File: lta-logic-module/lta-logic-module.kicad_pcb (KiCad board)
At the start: 2 copper layers, 63 parts, among them J1 Conn_01x01_Female, J2 Conn_01x01_Female, J3 Conn_01x12, J4 Conn_01x12, J5 Conn_01x12, U1 Feather_M4_Express, U10 PCF8574, U11 PCF8574, U12 PCF8574, U2 LM2595T-5, U3 SN74LVC14AD, U4 SN74LVC14AD, U5 SN74LVC00AD, U6 SN74LVC00AD, U7 SN74LVC244AN, U8 SN74LVC00AD, U9 SN74LVC00AD

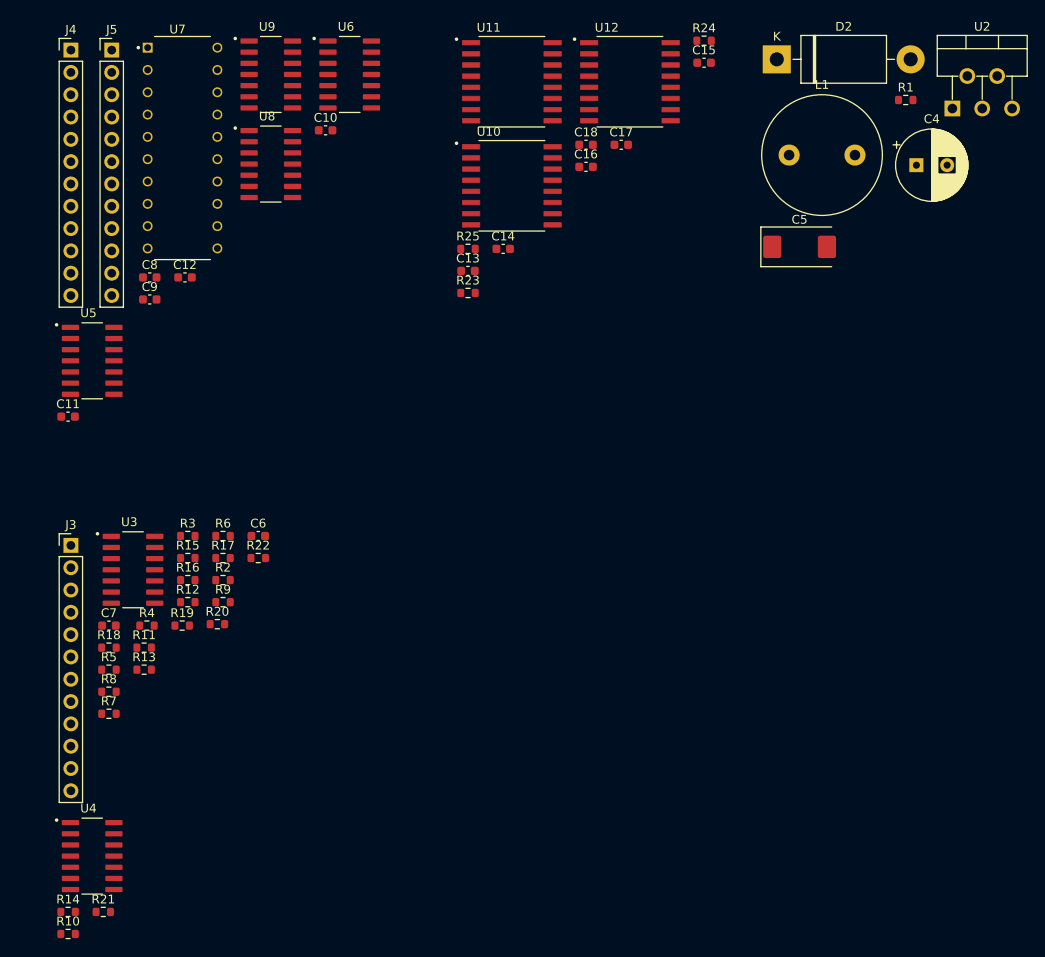
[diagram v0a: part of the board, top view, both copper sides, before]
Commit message: Initial PCB setup
* Configure Elecrow DRC checks for lta-logic-module.
* Switch SN74LVC244A from 'N' PDIP to 'DWR' SOIC footprint.
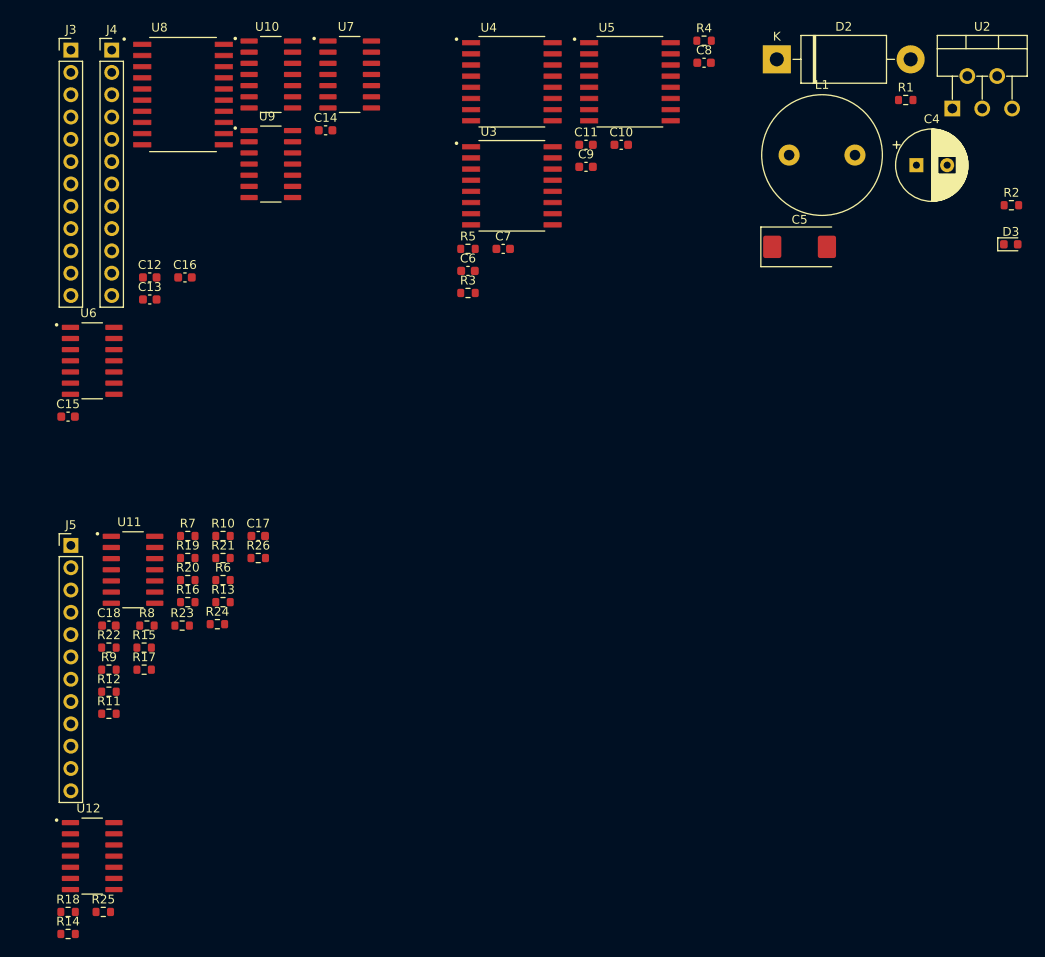
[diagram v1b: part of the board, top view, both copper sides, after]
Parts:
- removed the U7 at (131.9, 69.3)
- added D3: PWR (RED), LED_SMD:LED_0603_1608Metric, F.Cu at (226.2, 80.3)
- added R2: 330R, Resistor_SMD:R_0603_1608Metric, F.Cu at (226.2, 75.8)
- added U8: SN74LVC244ADW, Aaron_TI_Parts:TI_SOIC_DW0020A, F.Cu at (131.9, 63.2)
- renumbered C17 to C10, C18 to C11, C8 to C12, C9 to C13, C10 to C14, C11 to C15, C12 to C16, C6 to C17, C7 to C18, C13 to C6, C14 to C7, C15 to C8, C16 to C9, J4 to J3, J5 to J4, J3 to J5, R6 to R10, R7 to R11, R8 to R12, R9 to R13, R10 to R14, R11 to R15, R12 to R16, R13 to R17, R14 to R18, R15 to R19, R16 to R20, R17 to R21, R18 to R22, R19 to R23, R20 to R24, R21 to R25, R22 to R26, R23 to R3, R24 to R4, R25 to R5, R2 to R6, R3 to R7, R4 to R8, R5 to R9, U9 to U10, U3 to U11, U4 to U12, U10 to U3, U11 to U4, U12 to U5, U5 to U6, U6 to U7, U8 to U9

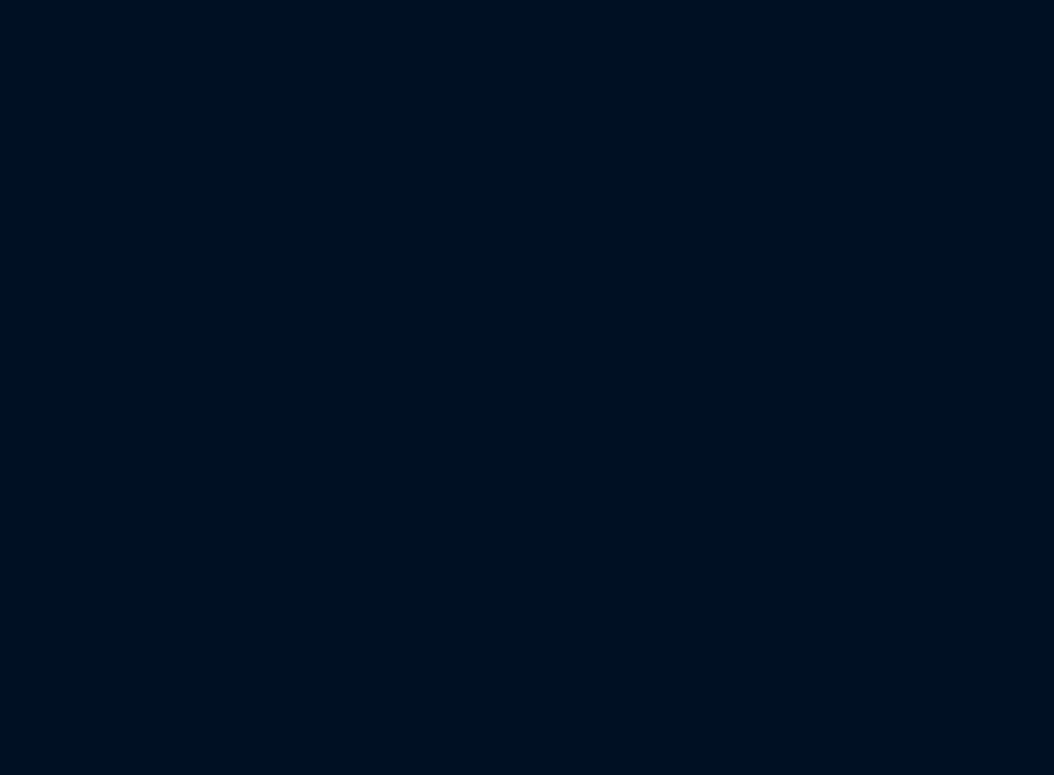
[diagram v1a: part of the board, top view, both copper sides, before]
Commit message: Add light sensor circuit.
Adjust TODOs and comments after testing btn circuit.
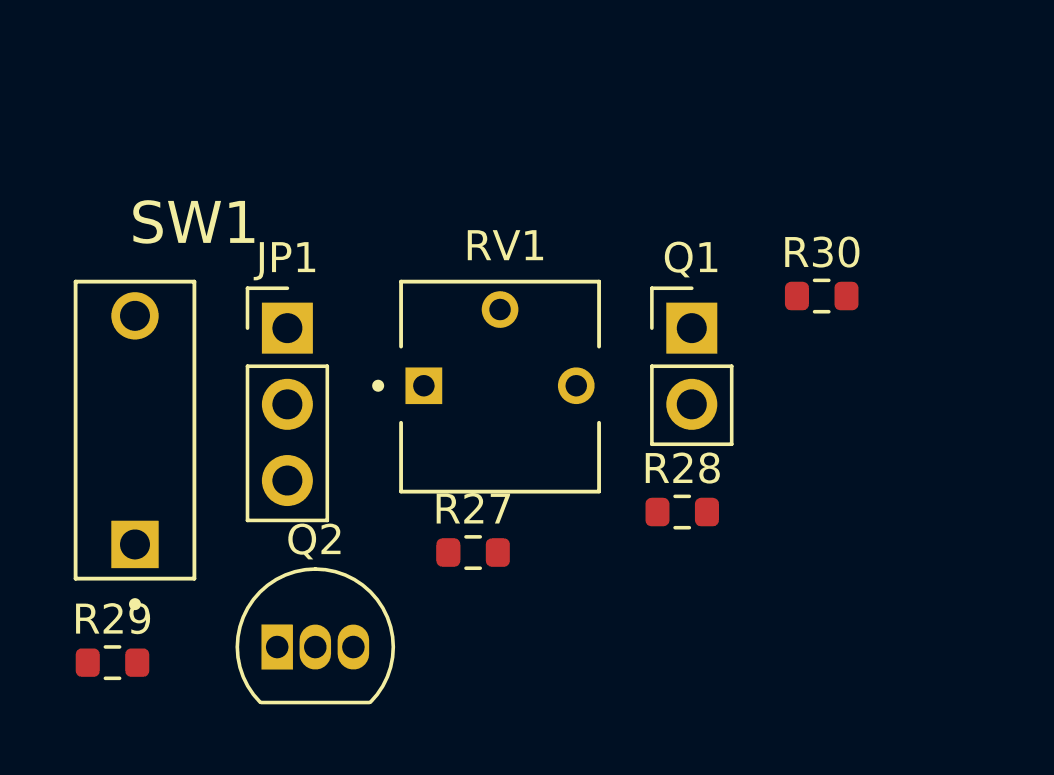
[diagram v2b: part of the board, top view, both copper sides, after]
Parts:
- added JP1: Jumper_3_Open, Connector_PinHeader_2.54mm:PinHeader_1x03_P2.54mm_Vertical, F.Cu at (58.8, 146.5)
- added Q1: PT334-6B, Connector_PinHeader_2.54mm:PinHeader_1x02_P2.54mm_Vertical, F.Cu at (72.2, 146.5)
- added Q2: KSC945CYTA, Package_TO_SOT_THT:TO-92_Inline, F.Cu at (58.4, 157.1)
- added R27: 4K7, Resistor_SMD:R_0603_1608Metric, F.Cu at (64.9, 154.0)
- added R28: 470R, Resistor_SMD:R_0603_1608Metric, F.Cu at (71.9, 152.6)
- added R29: 220R, Resistor_SMD:R_0603_1608Metric, F.Cu at (52.9, 157.7)
- added R30: 4K7, Resistor_SMD:R_0603_1608Metric, F.Cu at (76.6, 145.4)
- added RV1: 25K, Aaron_THT:TRIM_3362P, F.Cu at (65.8, 148.4)
- added SW1: SW_SPST, Aaron_THT:CUI-DIP-SW_DS01-254-x-01xx, F.Cu at (53.7, 149.9)
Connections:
- U1 pad 9: unconnected-(U1-Pad9) -> /DARK

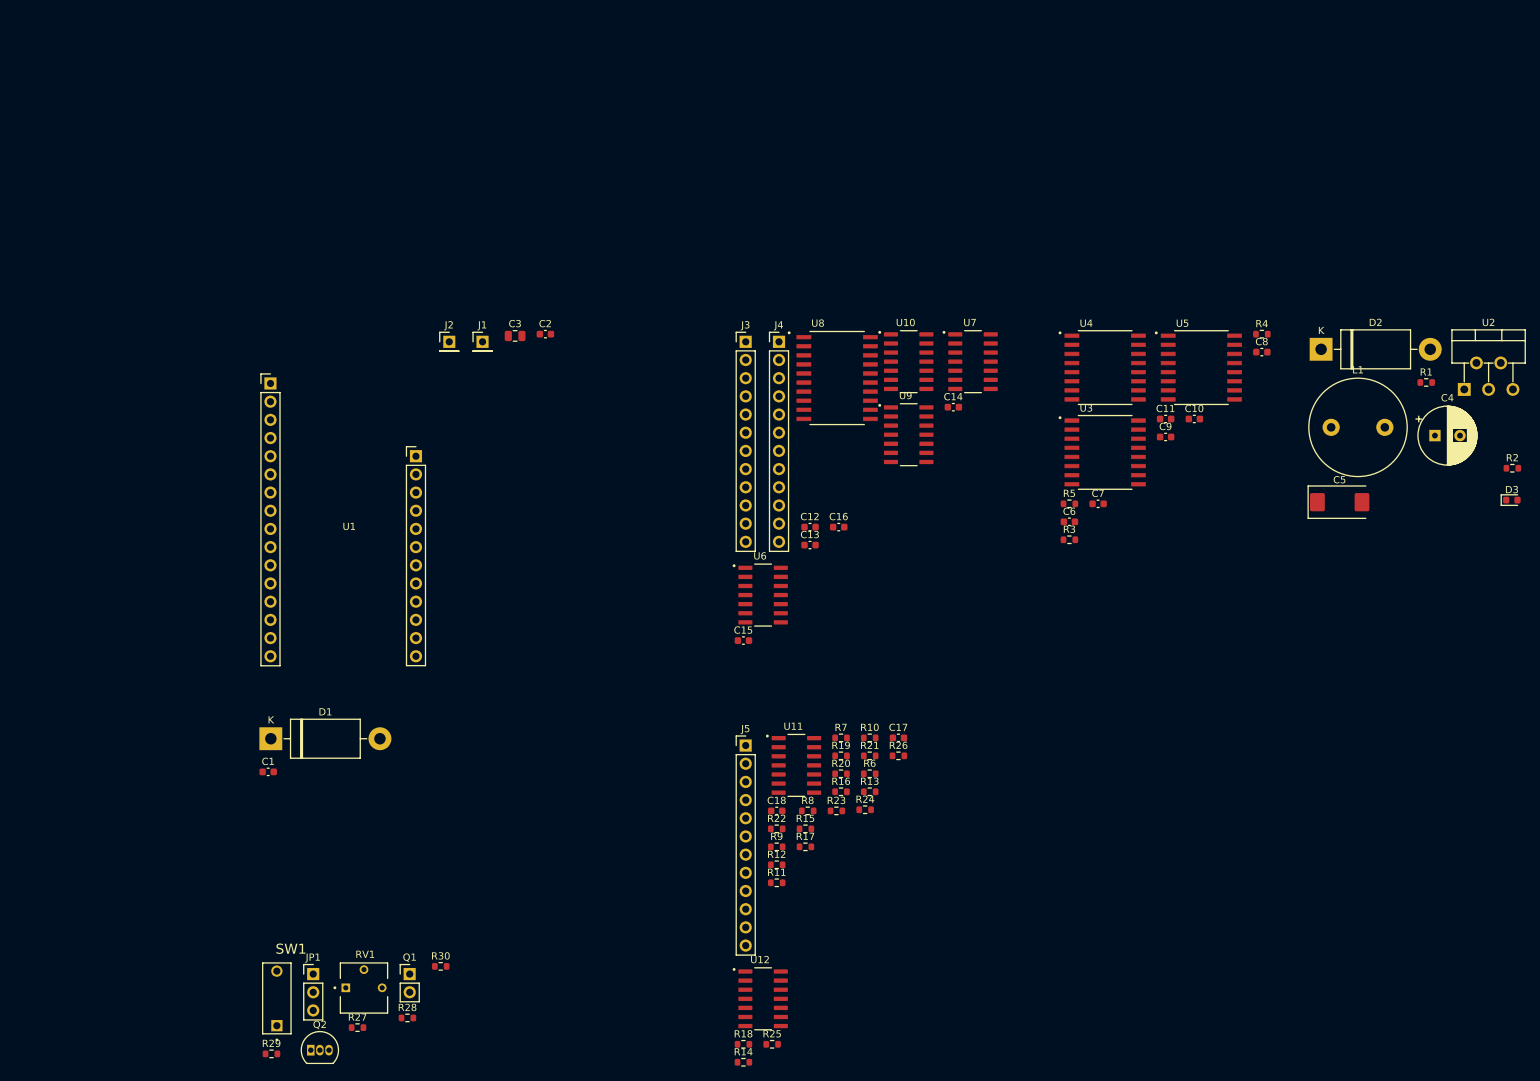
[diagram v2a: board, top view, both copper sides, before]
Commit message: Add main draft of PCB layout for logic module.
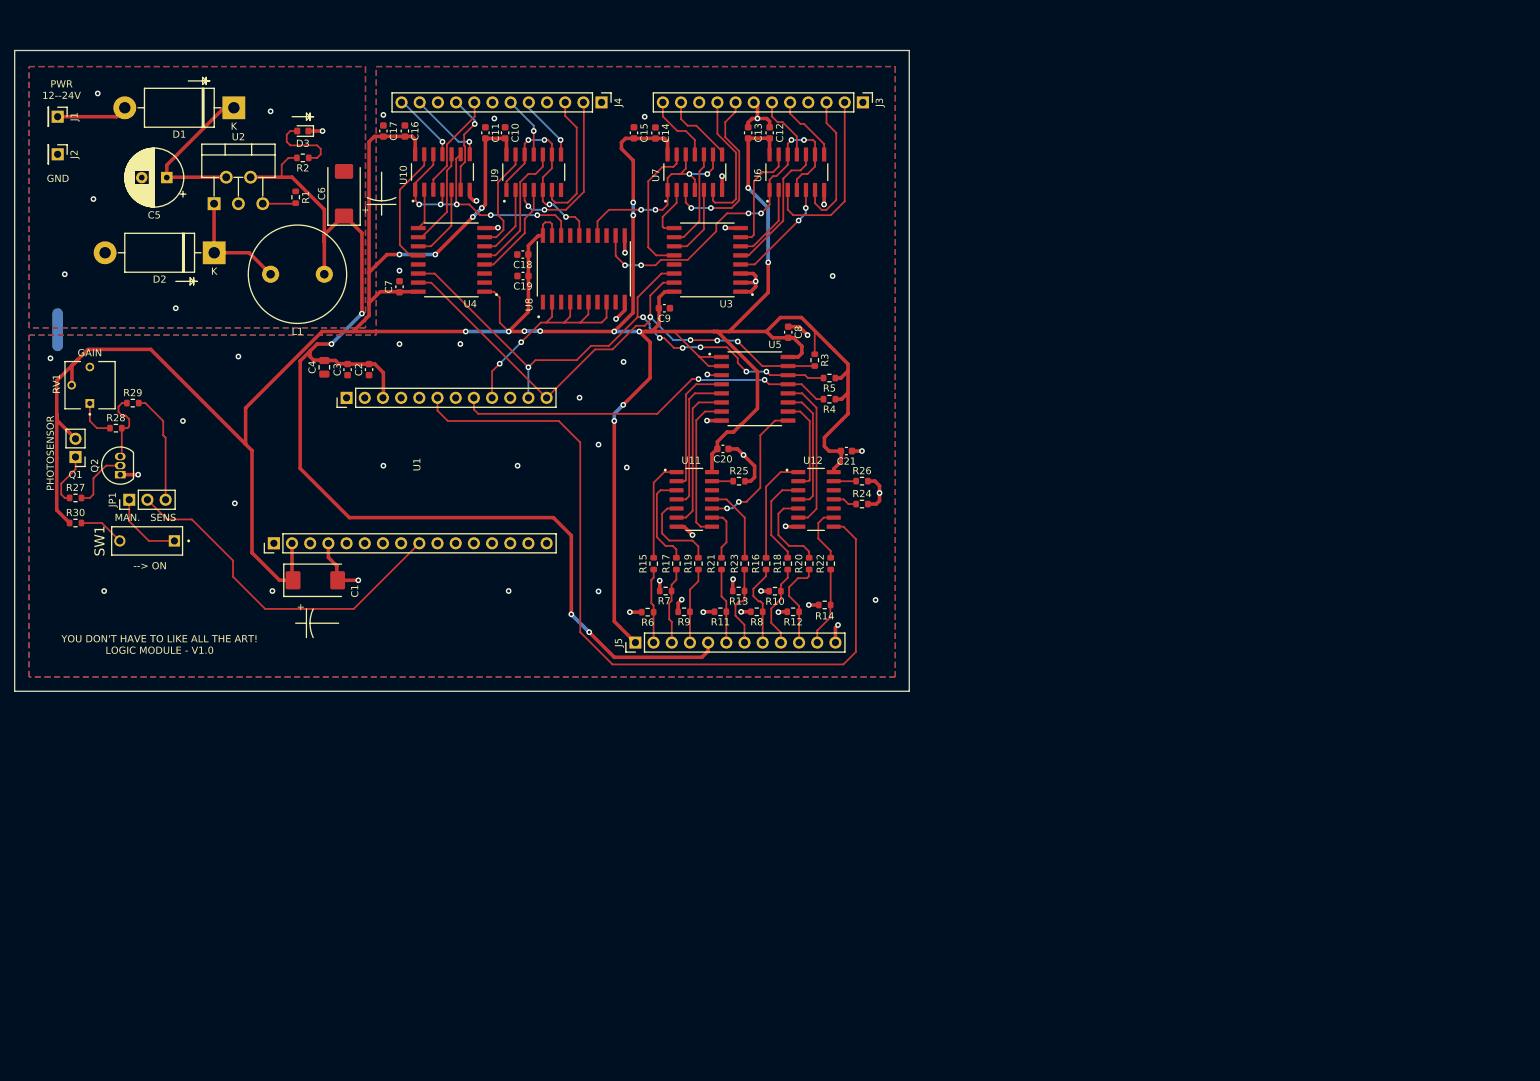
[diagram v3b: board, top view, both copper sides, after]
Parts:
- removed the C6 at (164.4, 83.3)
- removed the C7 at (168.4, 80.8)
- removed the C8 at (191.2, 59.6)
- added C1: 22u, Capacitor_Tantalum_SMD:CP_EIA-7343-30_AVX-N, F.Cu at (59.0, 91.5)
- added C11: 1u, Capacitor_SMD:C_0603_1608Metric, F.Cu at (82.8, 29.0)
- added C13: 1u, Capacitor_SMD:C_0603_1608Metric, F.Cu at (119.5, 29.0)
- added C15: 1u, Capacitor_SMD:C_0603_1608Metric, F.Cu at (103.5, 29.0)
- added C17: 1u, Capacitor_SMD:C_0603_1608Metric, F.Cu at (68.5, 28.8)
- added C18: 1u, Capacitor_SMD:C_0603_1608Metric, F.Cu at (88.0, 46.0)
- D3: value PWR (RED) -> PWR
- Q2: value KSC945CYTA -> 2N3904
- moved C5 180.8 mm to (38.3, 35.2), turned to 180 degrees
- moved D3 176.6 mm to (57.3, 28.8), turned to 180 degrees
- moved U2 176.5 mm to (44.9, 38.9)
- moved R2 174.4 mm to (57.3, 32.5), turned to 180 degrees
- moved R1 160.0 mm to (56.3, 38.0), turned to -90 degrees
- moved D2 155.2 mm to (44.9, 45.8), turned to 180 degrees
- moved C6 145.6 mm to (63.0, 37.5), turned to 90 degrees
- moved L1 142.7 mm to (60.0, 48.8), turned to 180 degrees
- moved C7 109.0 mm to (70.8, 50.5), turned to -90 degrees
- moved R29 92.9 mm to (33.5, 66.8)
- moved U4 92.5 mm to (78.0, 46.8), turned to 180 degrees
- moved RV1 92.5 mm to (27.6, 64.2), turned to 90 degrees
- moved R28 91.9 mm to (31.2, 70.2)
- moved D1 88.3 mm to (47.7, 25.5), turned to 180 degrees
- moved Q1 86.0 mm to (25.6, 74.3), turned to 180 degrees
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- renumbered C12 to C10, C13 to C12, C15 to C16, C16 to C19, C1 to C2, C17 to C20, C18 to C21, C2 to C3, C3 to C4, C4 to C5, C5 to C6, C9 to C7, C11 to C8, C10 to C9
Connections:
- net Net-(R15-Pad2) renamed /Button Inputs/btn_buf0
- net Net-(R16-Pad2) renamed /Button Inputs/btn_buf5
- net Net-(R17-Pad2) renamed /Button Inputs/btn_buf1
- net Net-(R18-Pad2) renamed /Button Inputs/btn_buf6
- net Net-(R19-Pad2) renamed /Button Inputs/btn_buf2
- net Net-(R20-Pad2) renamed /Button Inputs/btn_buf7
- net Net-(R21-Pad2) renamed /Button Inputs/btn_buf3
- net Net-(R22-Pad2) renamed /Button Inputs/btn_buf8
- net Net-(R23-Pad2) renamed /Button Inputs/btn_buf4
- U1 pad 22: /button8 -> unconnected-(U1-Pad22)
- U1 pad 23: unconnected-(U1-Pad23) -> /button8
- U3 pad 10: /led5 -> /led6
- U3 pad 11: /led6 -> /led5
- U3 pad 4: /led0 -> /led1
- U3 pad 5: /led1 -> /led2
- U3 pad 6: /led2 -> /led0
- U4 pad 10: /led13 -> /led14
- U4 pad 11: /led14 -> /led13
- U4 pad 4: /led8 -> /led9
- U4 pad 5: /led9 -> /led10
- U4 pad 6: /led10 -> /led8
- U8 pad 12: /LED Signal Outputs/EN3_L -> /LED Signal Outputs/EN0_L
- U8 pad 14: /LED Signal Outputs/EN2_L -> /LED Signal Outputs/EN1_L
- U8 pad 16: /LED Signal Outputs/EN1_L -> /LED Signal Outputs/EN2_L
- U8 pad 18: /LED Signal Outputs/EN0_L -> /LED Signal Outputs/EN3_L
- U9 pad 4: /LED Signal Outputs/EN2_L -> /led9
- U9 pad 5: /led9 -> /LED Signal Outputs/EN2_L
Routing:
- net +3V3: track 0.00 -> 496.2 mm, vias 0 -> 16
- net VDD: track 0.00 -> 162.1 mm, vias 0 -> 4
- net /button8: track 0.00 -> 110.7 mm
- net GND: track 0.00 -> 91.6 mm, vias 0 -> 57
- net /SCL: track 0.00 -> 82.8 mm, vias 0 -> 7
- net /SDA: track 0.00 -> 76.8 mm, vias 0 -> 4
- net /BUTTON_INT_L: track 0.00 -> 53.9 mm, vias 0 -> 2
- net /LED Signal Outputs/EN0_L: track 0.00 -> 51.1 mm, vias 0 -> 6
- net /DARK: track 0.00 -> 49.4 mm
- net /LED Signal Outputs/EN3_L: track 0.00 -> 40.8 mm, vias 0 -> 5
- net /LED_EN_L: track 0.00 -> 34.7 mm, vias 0 -> 2
- net /LED Signal Outputs/EN1_L: track 0.00 -> 31.2 mm, vias 0 -> 4
- net /LED Signal Outputs/EN2_L: track 0.00 -> 28.6 mm, vias 0 -> 4
- net /LED Signal Outputs/s0: track 0.00 -> 25.6 mm
- net /LED Signal Outputs/s4: track 0.00 -> 25.1 mm, vias 0 -> 2
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- added copper zone on B.Cu, net GND
- added copper zone on F.Cu, net GND
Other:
- board outline added: 125 x 89.5 mm
- board text added: "+"
- board text added: "--> ON"
- board text added: "<<< PROCESS DIRECTION >>>"
- board text added: "GAIN"
- board text added: "GND"
- board text added: "MAN."
- board text added: "PHOTOSENSOR"
- board text added: "PWR 12--24V"
- board text added: "SENS"
- board text added: "YOU DON'T HAVE TO LIKE ALL THE ART! LOGIC MODULE - V1.0"

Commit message: More unfucking.
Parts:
- removed J2: Conn_01x01_Female, Connector_PinHeader_2.54mm:PinHeader_1x01_P2.54mm_Vertical
- added FID1: Fiducial, Fiducial:Fiducial_1mm_Mask2mm, F.Cu at (25.3, 97.2)
- added FID2: Fiducial, Fiducial:Fiducial_1mm_Mask2mm, F.Cu at (137.3, 96.8)
- added FID3: Fiducial, Fiducial:Fiducial_1mm_Mask2mm, F.Cu at (136.3, 29.5)
- added H1: MountingHole_Pad, MountingHole:MountingHole_2.2mm_M2_ISO7380_Pad, F.Cu at (21.8, 102.2)
- added H2: MountingHole_Pad, MountingHole:MountingHole_2.2mm_M2_ISO7380_Pad, F.Cu at (137.3, 102.2)
- added H3: MountingHole_Pad, MountingHole:MountingHole_2.2mm_M2_ISO7380_Pad, F.Cu at (137.3, 22.2)
- added H4: MountingHole_Pad, MountingHole:MountingHole_2.2mm_M2_ISO7380_Pad, F.Cu at (21.8, 22.2)
- J1: value Conn_01x01_Female -> Molex-MicroFit_43650-0218; footprint Connector_PinHeader_2.54mm:PinHeader_1x01_P2.54mm_Vertical -> Aaron_THT:Molex-Microfit-43650-0218
- moved J1 5.97 mm to (25.9, 32.0), turned to 90 degrees
- moved C5 0.25 mm to (38.3, 35.0)
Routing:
- net GND: track 91.6 -> 96.5 mm
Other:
- board text added: "TODO FINALIZE MOUNTING HOLE ALIGNMENT"

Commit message: Switch 12-pin headers to Molex Micro-Latch c'tors.
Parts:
- J3, J4, J5: value Conn_01x12 -> Molex-MicroLatch-53253-1270; footprint Connector_PinHeader_2.54mm:PinHeader_1x12_P2.54mm_Vertical -> Aaron_THT:Molex-MicroLatch-53253-1270
- moved J3 6.30 mm to (129.3, 23.8), turned to 180 degrees
- moved J5 3.15 mm to (106.8, 101.0), turned to 0 degrees
- moved J4 2.90 mm to (96.3, 23.8), turned to 180 degrees
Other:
- board text added: "TODO: All connectors J3..J5 need their traces realigned"
- board text removed: "TODO FINALIZE MOUNTING HOLE ALIGNMENT"
